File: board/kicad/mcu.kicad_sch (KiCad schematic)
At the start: 33 parts, among them J3 SWD, U3 nRF52840-QIAA-R, U4 LIS2DH12TR, Y1 32 MHz CL=10pF, Y2 32.768 kHz CL=7pF

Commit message: Added microphone and battery contacts
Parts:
- added C47, C50, C52: 1u, Capacitor_SMD:C_0402_1005Metric, symbol Device:C_Small
- added C48: 330p, Capacitor_SMD:C_0402_1005Metric, symbol Device:C_Small
- added C49: 10u, Capacitor_SMD:C_0603_1608Metric, symbol Device:C_Small
- added C51: 4.7u, Capacitor_SMD:C_0402_1005Metric, symbol Device:C_Small
- added C53: 100n, Capacitor_SMD:C_0402_1005Metric, symbol Device:C_Small
- added C54: 10n, Capacitor_SMD:C_0402_1005Metric, symbol Device:C_Small
- added MK1: Capsule mic (original), cmd-z5:MIC_Contact_Concentric_D6.2mm, symbol Device:Microphone_Condenser
- added R19, R25: 1k, Resistor_SMD:R_0402_1005Metric, symbol Device:R_Small
- added R20, R24: 2.2k, Resistor_SMD:R_0402_1005Metric, symbol Device:R_Small
- added R21, R22, R23, R26: 100k, Resistor_SMD:R_0402_1005Metric, symbol Device:R_Small
- added U8: TLV9001IDCKR, Package_TO_SOT_SMD:SOT-353_SC-70-5, symbol Amplifier_Operational:TLV9001IDCK
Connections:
- net GND: now also C49.2, C50.2, C51.2, C52.2, C53.2, C54.2, MK1.1 (-), R26.2, U8.2 (V-)
- net MIC_OUT: now reaches U3.K2 (AIN3/P0.05)
- net MIC_OUT: now also C54.1, R25.2
- new net MIC_AMP: C48.2, R23.2, R25.1, U8.4
- new net MIC_BIAS: C49.1, R19.2, R20.1
- new net MIC_FB: C48.1, R23.1, R24.2, U8.3 (-)
- new net MIC_IN: C47.1, MK1.2 (+), R20.2
- new net MIC_INP: C47.2, R22.2, U8.1 (+)
- new net MIC_RG: C51.1, R24.1
- new net MIC_VDD: C52.1, C53.1, R19.1, R21.1, U8.5 (V+)
- new net MIC_VREF: C50.1, R21.2, R22.1, R26.1
- no-connect marks 6 -> 5
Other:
- note added: "Inner pad = MIC_IN, outer ring = GND. MIC_VDD from nPM1300 GPIO1 (6 mA drive, high = on, off in low-power mode). Bias 1k + 10u filter, 2.2k load (~2 V on mic). Gain 33 dB, 15 Hz - 4.8 kHz; MIC_OUT idles at VDD/2 -> SAADC AIN3 (P0.05), single-ended."
- note added: "Microphone (original capsule)"
- note added: "P0.04: spare (AIN2), P0.05 (AIN3): microphone DEC2, DEC5: not connected (aQFN73 build code Fxx and later)"
- note removed: "P0.04 / P0.05: spare (AIN2/AIN3) DEC2, DEC5: not connected (aQFN73 build code Fxx and later)"

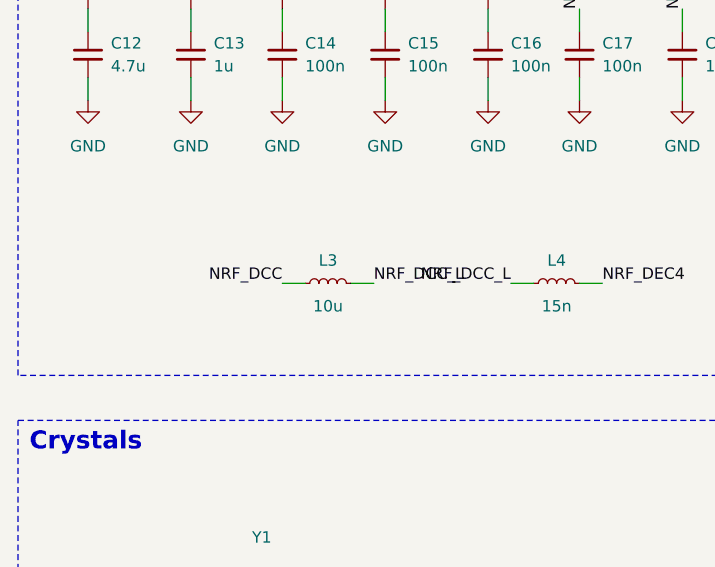
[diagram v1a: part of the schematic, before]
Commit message: Optimized placement
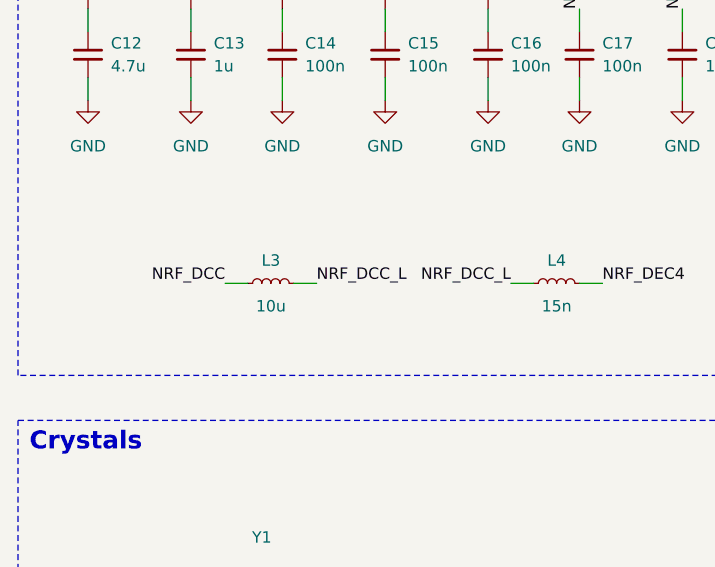
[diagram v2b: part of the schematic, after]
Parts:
- Y2: footprint Crystal:Crystal_SMD_2012-2Pin_2.0x1.2mm -> cmd-z5:Crystal_SMD_2012-2Pin_2.0x1.2mm
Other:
- moved on the sheet: L3
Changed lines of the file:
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@@
 	(wire
 		(pts
-			(xy 46.99 64.77) (xy 49.53 64.77)
+			(xy 40.64 64.77) (xy 43.18 64.77)
 		)
 		(stroke
@@
 	(wire
 		(pts
-			(xy 41.91 64.77) (xy 39.37 64.77)
+			(xy 35.56 64.77) (xy 33.02 64.77)
 		)
 		(stroke
@@
 	)
 	(label "NRF_DCC_L"
-		(at 49.53 64.77 0)
+		(at 43.18 64.77 0)
 		(effects
 			(font
@@
 	)
 	(label "NRF_DCC"
-		(at 39.37 64.77 180)
+		(at 33.02 64.77 180)
 		(effects
 			(font
@@
 			)
 		)
-		(property "Footprint" "Crystal:Crystal_SMD_2012-2Pin_2.0x1.2mm"
+		(property "Footprint" "cmd-z5:Crystal_SMD_2012-2Pin_2.0x1.2mm"
 			(at 100.33 100.33 0)
 			(hide yes)
@@
 	(symbol
 		(lib_id "Device:L_Small")
-		(at 44.45 64.77 90)
+		(at 38.1 64.77 90)
 		(unit 1)
 		(body_style 1)
@@
 		(dnp no)
 		(property "Reference" "L3"
-			(at 44.45 62.23 90)
+			(at 38.1 62.23 90)
 			(show_name no)
 			(do_not_autoplace no)
@@
 		)
 		(property "Value" "10u"
-			(at 44.45 67.31 90)
+			(at 38.1 67.31 90)
 			(show_name no)
 			(do_not_autoplace no)
@@
 		)
 		(property "Footprint" "Inductor_SMD:L_0603_1608Metric"
-			(at 44.45 64.77 90)
+			(at 38.1 64.77 90)
 			(hide yes)
 			(show_name no)
@@
 		)
 		(property "Datasheet" ""
-			(at 44.45 64.77 90)
+			(at 38.1 64.77 90)
 			(hide yes)
 			(show_name no)
@@
 		)
 		(property "Description" "Inductor, small symbol"
-			(at 44.45 64.77 90)
+			(at 38.1 64.77 90)
 			(hide yes)
 			(show_name no)
